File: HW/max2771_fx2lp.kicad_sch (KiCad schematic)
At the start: 53 parts, among them J1 SMA-ANG, J2 SMA-ANG, J3 Screw_Terminal_01x02, J4 SMA-ANG, P1 Conn_02x10_Odd_Even, P2 Conn_02x10_Odd_Even, U1 MAX2771, U2 MAX2771

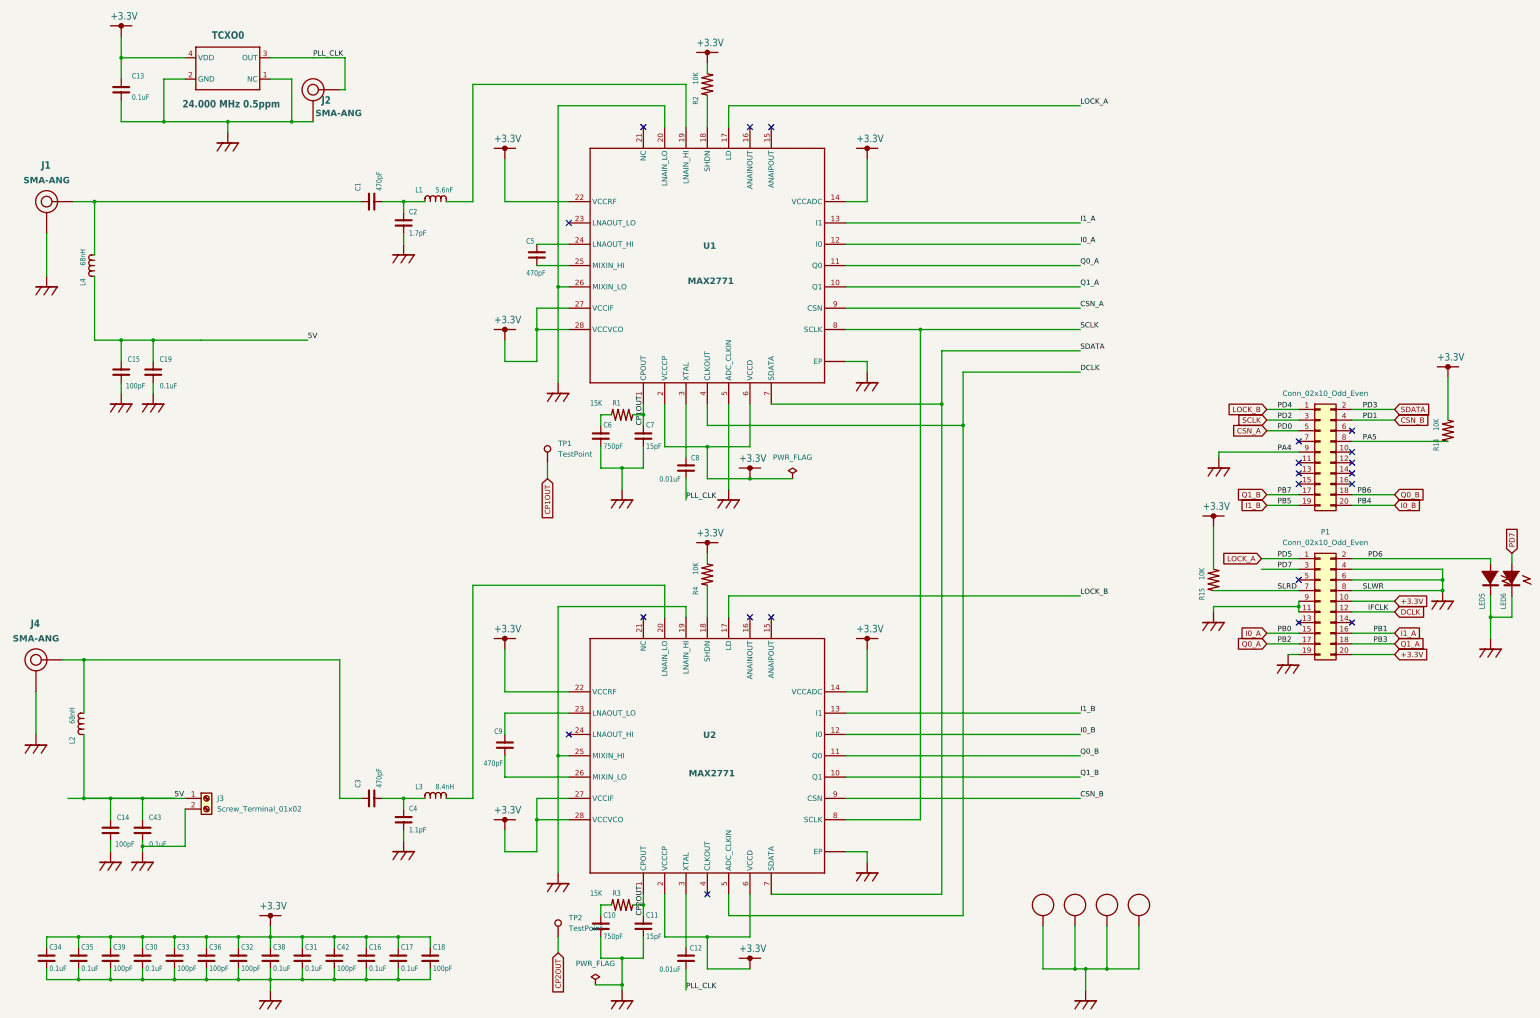
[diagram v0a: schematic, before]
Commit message: add option for feeding either Hi or Lo frequency band
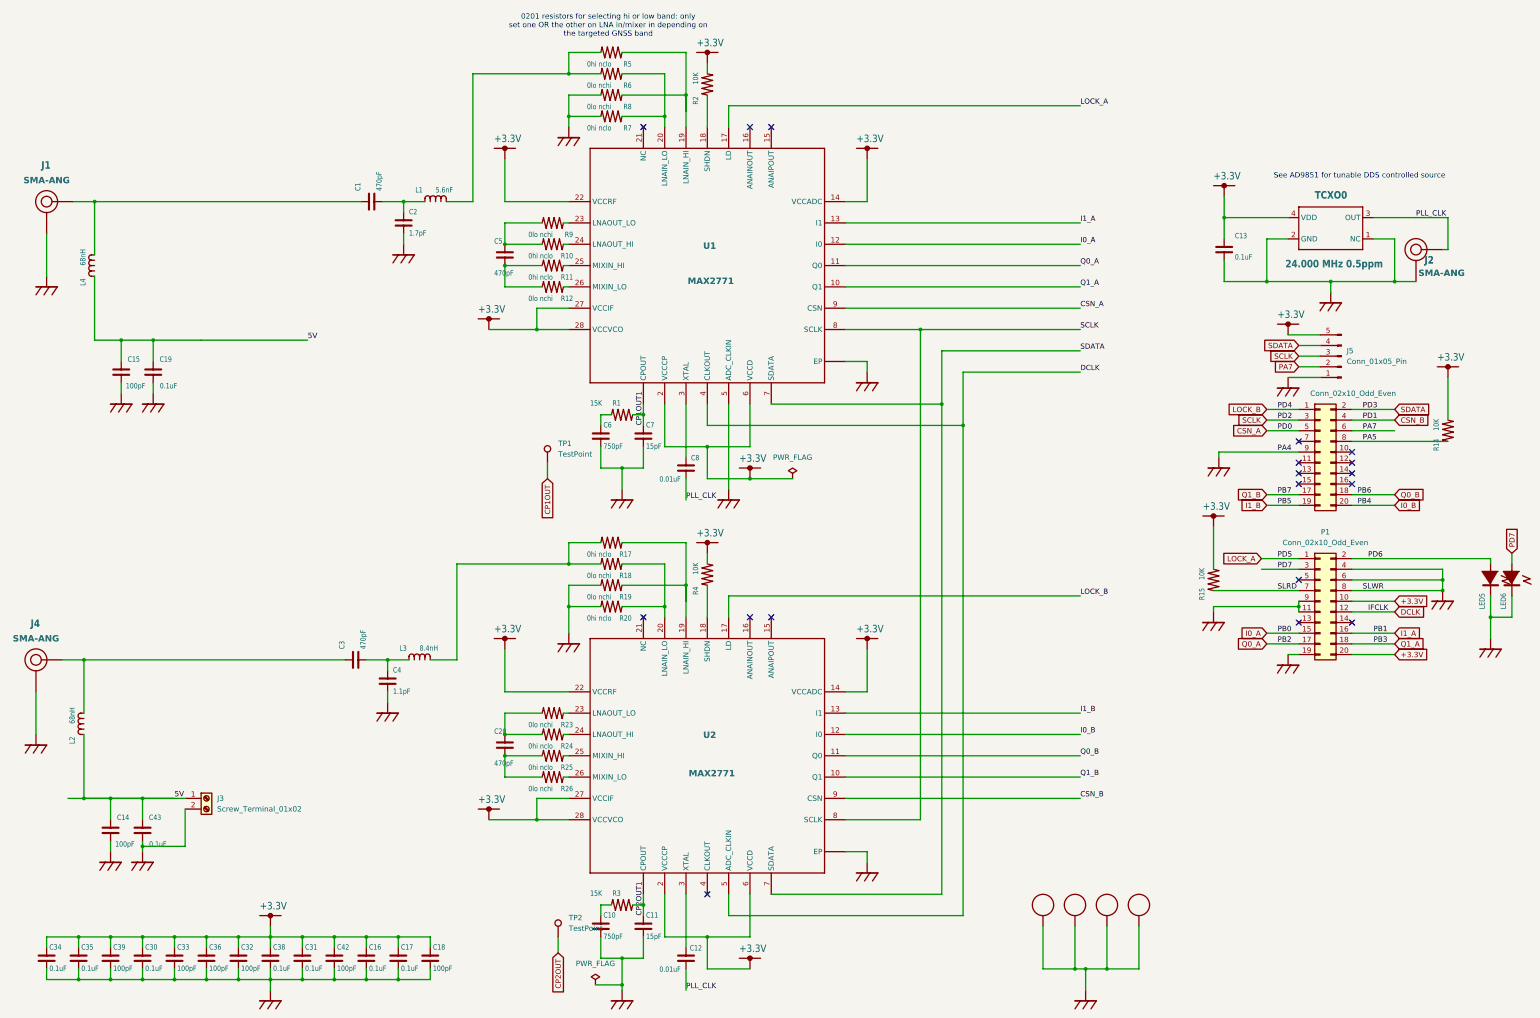
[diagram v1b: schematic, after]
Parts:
- removed C9: 470pF, pocket_sdr_v2.3:C1005, symbol pocket_sdr_v2.3-eagle-import:C1005
- added C20: 470pF, pocket_sdr_v2.3:C1005, symbol pocket_sdr_v2.3-eagle-import:C1005
- added J5: Conn_01x05_Pin, Connector_PinHeader_2.54mm:PinHeader_1x05_P2.54mm_Vertical, symbol Connector:Conn_01x05_Pin
- added R10, R11, R17, R20, R24, R25, R5, R7: 0hi nclo, Resistor_SMD:R_0201_0603Metric, symbol pocket_sdr_v2.3-eagle-import:R1005
- added R12, R18, R19, R23, R26, R6, R8, R9: 0lo nchi, Resistor_SMD:R_0201_0603Metric, symbol pocket_sdr_v2.3-eagle-import:R1005
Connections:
- net +3.3V: now also J5.5 (Pin_5)
- net CPAD_2.2MM: now also J5.1 (Pin_1), R19.2 (P$2), R20.2 (P$2), R7.2 (P$2), R8.2 (P$2); no longer U1.20 (LNAIN_LO), U1.26 (MIXIN_LO), U2.19 (LNAIN_HI), U2.25 (MIXIN_HI)
- net SCLK: now also J5.3 (Pin_3)
- net SDATA: now also J5.4 (Pin_4)
- net at U2.20 (LNAIN_LO): now also R18.1 (P$1), R20.1 (P$1); no longer L3.2 (P$2)
- net at U2.23 (LNAOUT_LO): now also R23.1 (P$1)
- net at U2.24 (LNAOUT_HI): now also R24.1 (P$1)
- net at U2.26 (MIXIN_LO): now also R26.1 (P$1)
- net at U1.19 (LNAIN_HI): now also R5.1 (P$1), R8.1 (P$1); no longer L1.2 (P$2)
- net at U1.24 (LNAOUT_HI): now also R10.1 (P$1); no longer C5.1
- net at C5.2: now also R11.2 (P$2), R12.2 (P$2); no longer U1.25 (MIXIN_HI)
- net PA7: now reaches P2.6 (Pin_6)
- net PA7: now also J5.2 (Pin_2)
- net at U1.23 (LNAOUT_LO): now also R9.1 (P$1)
- new net: C5.1, R10.2 (P$2), R9.2 (P$2)
- new net: L1.2 (P$2), R5.2 (P$2), R6.2 (P$2)
- new net: C20.1, R23.2 (P$2), R24.2 (P$2)
- new net: C20.2, R25.2 (P$2), R26.2 (P$2)
- new net: R25.1 (P$1), U2.25 (MIXIN_HI)
- new net: R6.1 (P$1), R7.1 (P$1), U1.20 (LNAIN_LO)
- new net: R17.1 (P$1), R19.1 (P$1), U2.19 (LNAIN_HI)
- new net: L3.2 (P$2), R17.2 (P$2), R18.2 (P$2)
- new net: R11.1 (P$1), U1.25 (MIXIN_HI)
- new net: R12.1 (P$1), U1.26 (MIXIN_LO)
- no-connect marks 21 -> 18
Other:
- note added: "0201 resistors for selecting hi or low band: only set one OR the other on LNA in/mixer in depending on the targeted GNSS band"
- note added: "See AD9851 for tunable DDS controlled source"
- moved on the sheet: C13, C3, C4, C5, J2, L3, TCXO0

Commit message: mirror connectors
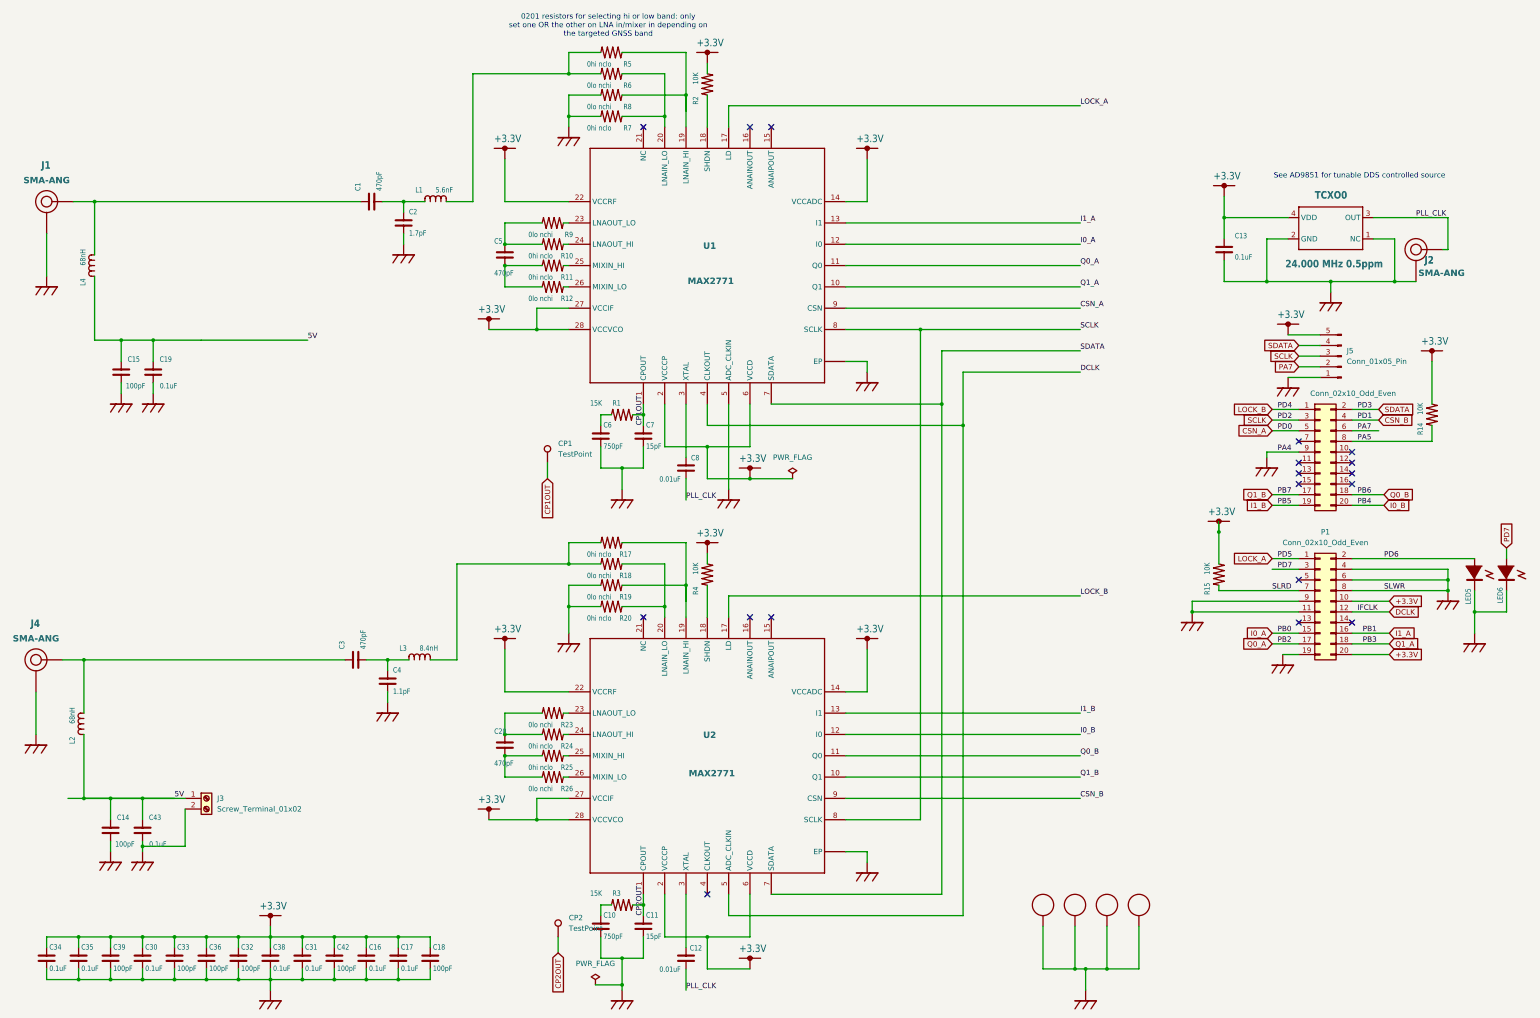
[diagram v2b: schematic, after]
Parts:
- renumbered TP1 to CP1, TP2 to CP2
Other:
- moved on the sheet: LED5, LED6, R14, R15

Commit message: update documentation/Makefile
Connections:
- net 5V: now also C1.1, J1.P1 (RF), L4.2 (P$2)
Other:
- moved on the sheet: C14, C15, C16, C17, C18, C19, C3, C30, C31, C32, C33, C34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

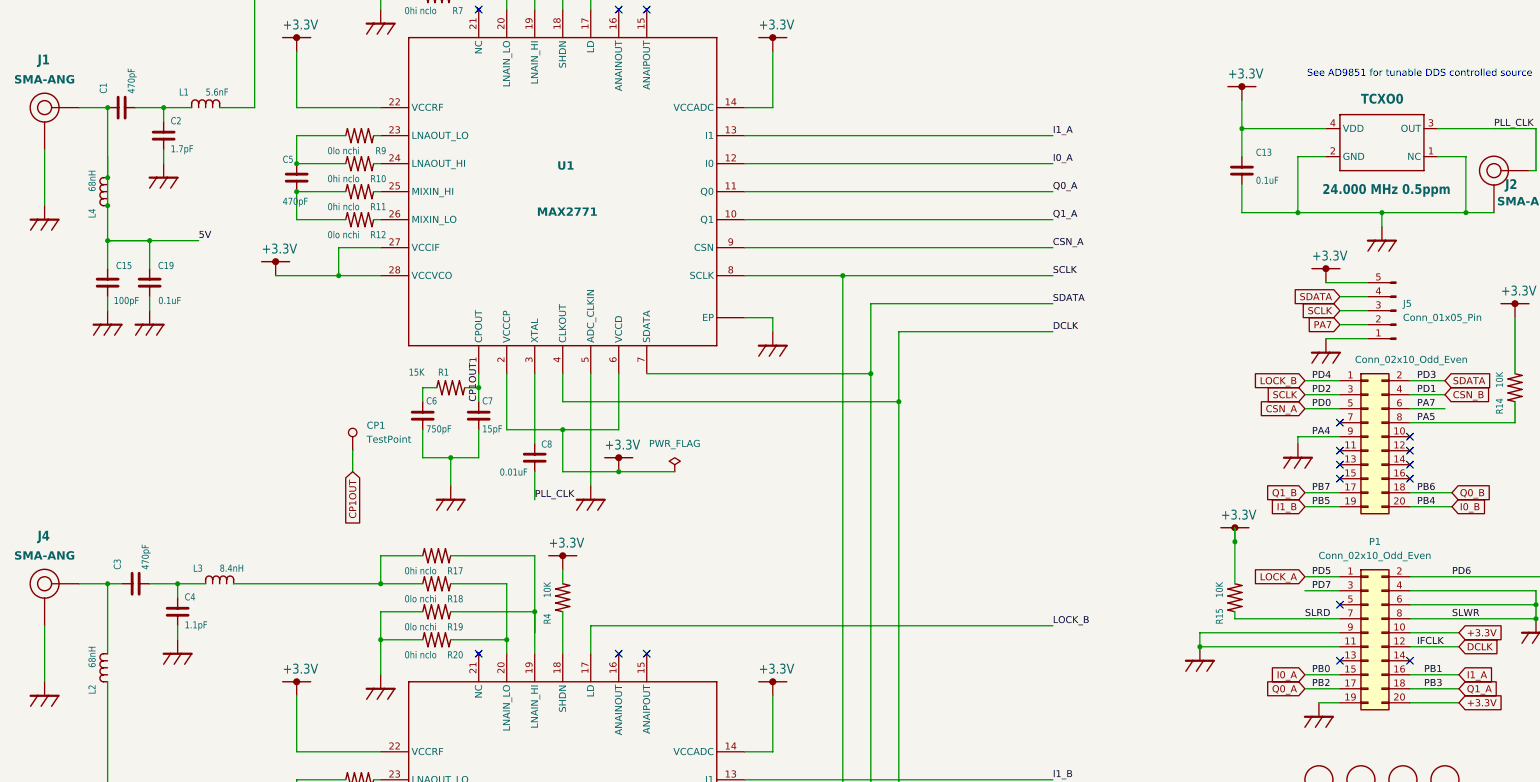
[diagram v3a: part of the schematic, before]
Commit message: add SMA 3D model
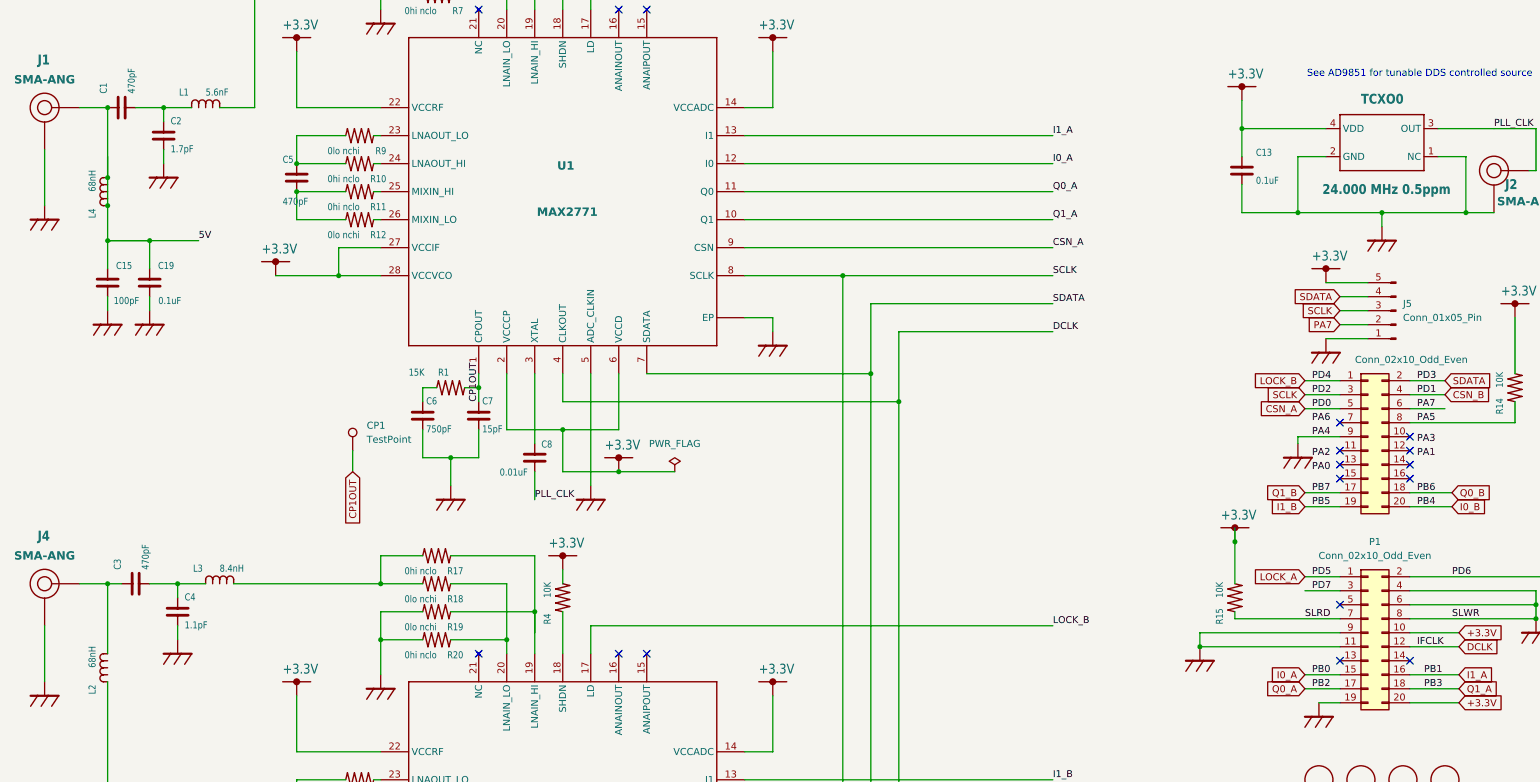
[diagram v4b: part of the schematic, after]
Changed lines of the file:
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@@
 (kicad_sch
-	(version 20231120)
+	(version 20250114)
 	(generator "eeschema")
-	(generator_version "8.0")
+	(generator_version "9.0")
 	(paper "User" 499.999 319.989)
+	(text "0201 resistors for selecting hi or low band: only\nset one OR the other on LNA in/mixer in depending on \nthe targeted GNSS band"
+		(exclude_from_sim no)
+		(at 145.288 50.8 0)
+		(effects
+			(font
+				(size 1.27 1.27)
+			)
+		)
+	)
+	(text "See AD9851 for tunable DDS controlled source"
+		(exclude_from_sim no)
+		(at 324.358 86.614 0)
+		(effects
+			(font
+				(size 1.27 1.27)
+			)
+		)
+	)
 	(junction
 		(at 316.23 229.87)
@@
 		)
 	)
-	(text "0201 resistors for selecting hi or low band: only\nset one OR the other on LNA in/mixer in depending on \nthe targeted GNSS band"
-		(exclude_from_sim no)
-		(at 145.288 50.8 0)
-		(effects
-			(font
-				(size 1.27 1.27)
-			)
-		)
-	)
-	(text "See AD9851 for tunable DDS controlled source"
-		(exclude_from_sim no)
-		(at 324.358 86.614 0)
-		(effects
-			(font
-				(size 1.27 1.27)
-			)
-		)
-	)
 	(label "PA7"
 		(at 323.85 147.32 0)
-		(fields_autoplaced yes)
 		(effects
 			(font
@@
 	(label "PD4"
 		(at 304.8 142.24 0)
-		(fields_autoplaced yes)
 		(effects
 			(font
@@
 	(label "PLL_CLK"
 		(at 163.83 280.67 0)
-		(fields_autoplaced yes)
 		(effects
 			(font
@@
 	(label "PA4"
 		(at 304.8 152.4 0)
-		(fields_autoplaced yes)
 		(effects
 			(font
@@
 	(label "CSN_B"
 		(at 257.81 234.95 0)
-		(fields_autoplaced yes)
 		(effects
 			(font
@@
 	(label "Q1_A"
 		(at 257.81 113.03 0)
-		(fields_autoplaced yes)
 		(effects
 			(font
@@
 	(label "PB2"
 		(at 304.8 198.12 0)
-		(fields_autoplaced yes)
 		(effects
 			(font
@@
 	(label "I1_A"
 		(at 257.81 97.79 0)
-		(fields_autoplaced yes)
 		(effects
 			(font
@@
 		)
 	)
+	(label "PA1"
+		(at 323.85 156.21 0)
+		(effects
+			(font
+				(size 1.27 1.27)
+			)
+			(justify left bottom)
+		)
+	)
+	(label "PA2"
+		(at 304.8 156.21 0)
+		(effects
+			(font
+				(size 1.27 1.27)
+			)
+			(justify left bottom)
+		)
+	)
+	(label "PA6"
+		(at 304.8 149.86 0)
+		(effects
+			(font
+				(size 1.27 1.27)
+			)
+			(justify left bottom)
+		)
+	)
 	(label "PD2"
 		(at 304.8 144.78 0)
-		(fields_autoplaced yes)
 		(effects
 			(font
@@
 	(label "PD7"
 		(at 304.8 180.34 0)
-		(fields_autoplaced yes)
 		(effects
 			(font
@@
 	(label "PLL_CLK"
 		(at 163.83 163.83 0)
-		(fields_autoplaced yes)
 		(effects
 			(font
@@
 	(label "5V"
 		(at 102.87 116.84 0)
-		(fields_autoplaced yes)
 		(effects
 			(font
@@
 	(label "PB4"
 		(at 323.85 165.1 0)
-		(fields_autoplaced yes)
 		(effects
 			(font
@@
 	(label "PB7"
 		(at 304.8 162.56 0)
-		(fields_autoplaced yes)
 		(effects
 			(font
@@
 	(label "PD3"
 		(at 323.85 142.24 0)
-		(fields_autoplaced yes)
+		(effects
+			(font
+				(size 1.27 1.27)
+			)
+			(justify left bottom)
+		)
+	)
+	(label "PA3"
+		(at 323.85 153.67 0)
 		(effects
 			(font
@@
 	(label "Q0_A"
 		(at 257.81 107.95 0)
-		(fields_autoplaced yes)
 		(effects
 			(font
@@
 	(label "IFCLK"
 		(at 323.85 190.5 0)
-		(fields_autoplaced yes)
 		(effects
 			(font
@@
 	(label "CP1OUT"
 		(at 153.67 146.05 90)
-		(fields_autoplaced yes)
 		(effects
 			(font
@@
 	(label "SLRD"
 		(at 303.53 185.42 0)
-		(fields_autoplaced yes)
 		(effects
 			(font
@@
 	(label "SLWR"
 		(at 330.2 185.42 0)
-		(fields_autoplaced yes)
 		(effects
 			(font
@@
 	(label "I1_B"
 		(at 257.81 214.63 0)
-		(fields_autoplaced yes)
 		(effects
 			(font
@@
 	(label "I0_A"
 		(at 257.81 102.87 0)
-		(fields_autoplaced yes)
 		(effects
 			(font
@@
 	(label "DCLK"
 		(at 257.81 133.35 0)
-		(fields_autoplaced yes)
 		(effects
 			(font
@@
 	(label "PLL_CLK"
 		(at 337.82 96.52 0)
-		(fields_autoplaced yes)
 		(effects
 			(font
@@
 	(label "Q1_B"
 		(at 257.81 229.87 0)
-		(fields_autoplaced yes)
 		(effects
 			(font
@@
 		)
 	)
+	(label "PA0"
+		(at 304.8 158.75 0)
+		(effects
+			(font
+				(size 1.27 1.27)
+			)
+			(justify left bottom)
+		)
+	)
 	(label "PB1"
 		(at 325.12 195.58 0)
-		(fields_autoplaced yes)
 		(effects
 			(font
@@
 	(label "CP2OUT"
 		(at 153.67 262.89 90)
-		(fields_autoplaced yes)
 		(effects
 			(font
@@
 	(label "LOCK_B"
 		(at 257.81 186.69 0)
-		(fields_autoplaced yes)
 		(effects
 			(font
@@
 	(label "SDATA"
 		(at 257.81 128.27 0)
-		(fields_autoplaced yes)
 		(effects
 			(font
@@
 	(label "SCLK"
 		(at 257.81 123.19 0)
-		(fields_autoplaced yes)
 		(effects
 			(font
@@
 	(label "Q0_B"
 		(at 257.81 224.79 0)
-		(fields_autoplaced yes)
 		(effects
 			(font
@@
 	(label "PD0"
 		(at 304.8 147.32 0)
-		(fields_autoplaced yes)
 		(effects
 			(font
@@
 	(label "PA5"
 		(at 323.85 149.86 0)
-		(fields_autoplaced yes)
 		(effects
 			(font
@@
 	(label "PD5"
 		(at 304.8 177.8 0)
-		(fields_autoplaced yes)
 		(effects
 			(font
@@
 	(label "CSN_A"
 		(at 257.81 118.11 0)
-		(fields_autoplaced yes)
 		(effects
 			(font
@@
 	(label "PD6"
 		(at 330.2 177.8 0)
-		(fields_autoplaced yes)
 		(effects
 			(font
@@
 	(label "PB6"
 		(at 323.85 162.56 0)
-		(fields_autoplaced yes)
 		(effects
 			(font
@@
 	(label "I0_B"
 		(at 257.81 219.71 0)
-		(fields_autoplaced yes)
 		(effects
 			(font
@@
 	(label "PD1"
 		(at 323.85 144.78 0)
-		(fields_autoplaced yes)
 		(effects
 			(font
@@
 	(label "PB3"
 		(at 325.12 198.12 0)
-		(fields_autoplaced yes)
 		(effects
 			(font
@@
 	(label "LOCK_A"
 		(at 257.81 69.85 0)
-		(fields_autoplaced yes)
 		(effects
 			(font
@@
 	(label "PB0"
 		(at 304.8 195.58 0)
-		(fields_autoplaced yes)
 		(effects
 			(font
@@
 	(label "5V"
 		(at 97.79 234.95 0)
-		(fields_autoplaced yes)
 		(effects
 			(font
@@
 	(label "PB5"
 		(at 304.8 165.1 0)
-		(fields_autoplaced yes)
 		(effects
 			(font
@@
 		)
 	)
+	(embedded_fonts no)
 )
